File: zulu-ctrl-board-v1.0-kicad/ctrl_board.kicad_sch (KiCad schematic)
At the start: 34 parts, among them J1 Zulu I2C w/ interrupt Connect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, J2 OLED Connector, J305 I2C Qwiic, J5 CENTER_INT, J8 Zulu I2C w/ interrupt Connect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, SW1 SW_SPST, SW2 SW_SPST, SW4 Rotary_Encoder_Switch, U1 PCA9554APW,118

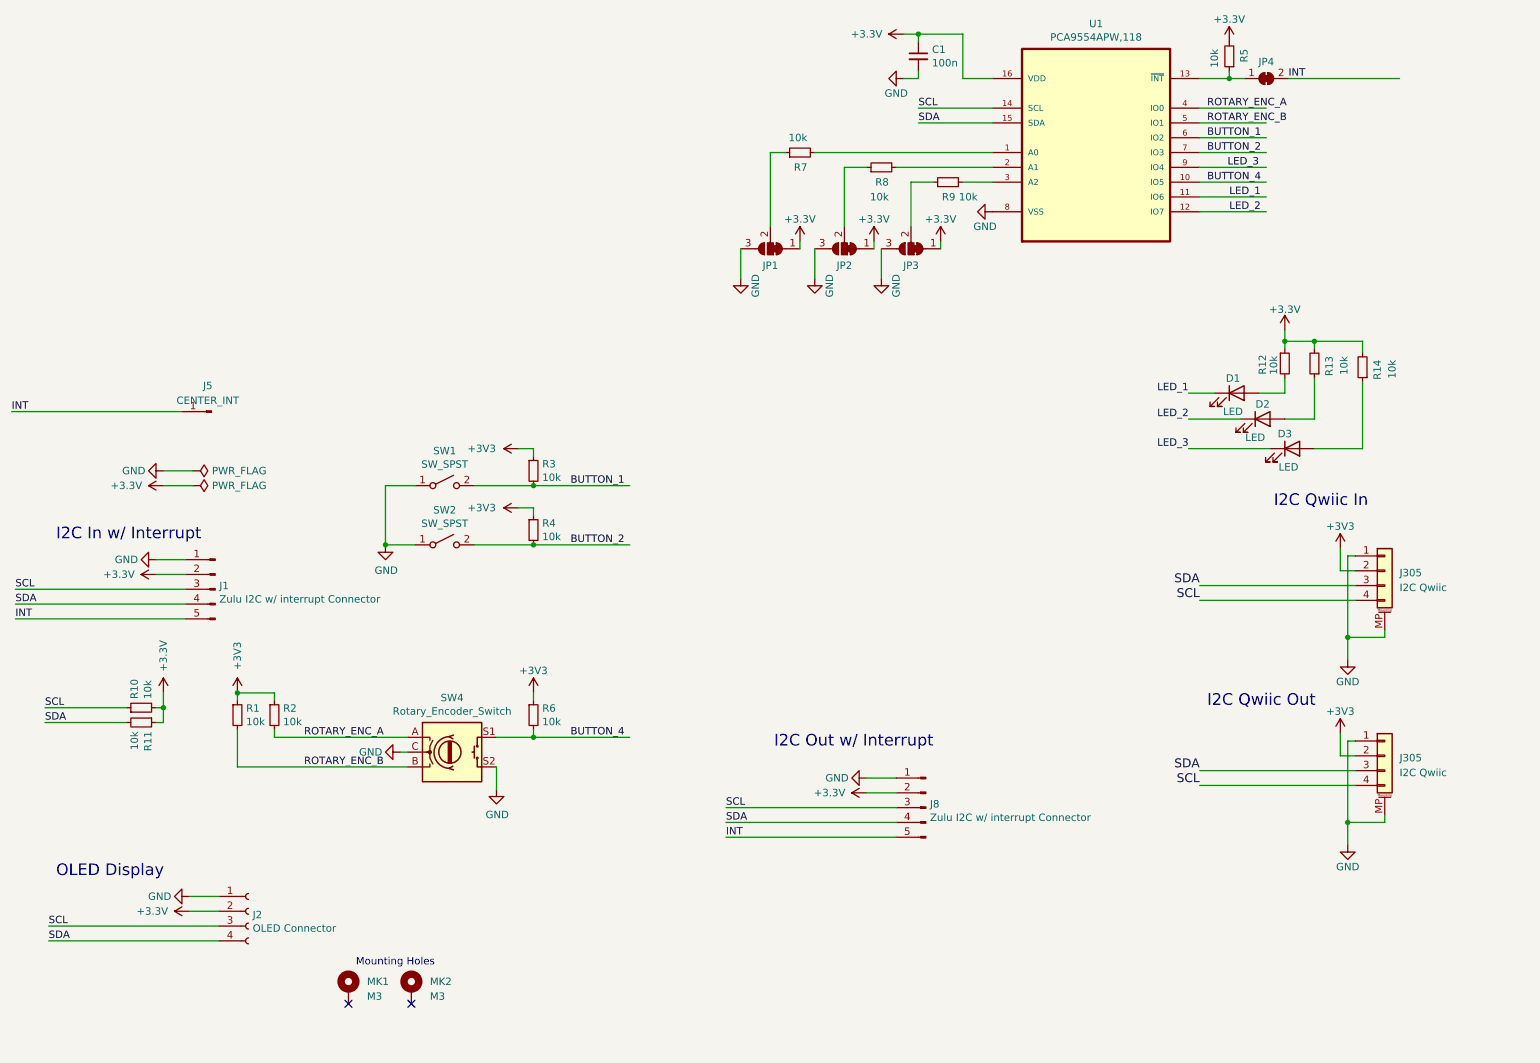
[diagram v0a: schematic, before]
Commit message: Design of new rev
Dropped 2.54mm pitch I2C headers, except for display
Removed LEDs
Added two more mounting holes. Made all 4 of them 2.8mm holes
Decreased the size of the board
Moved buttons, rotary, and screen closer together
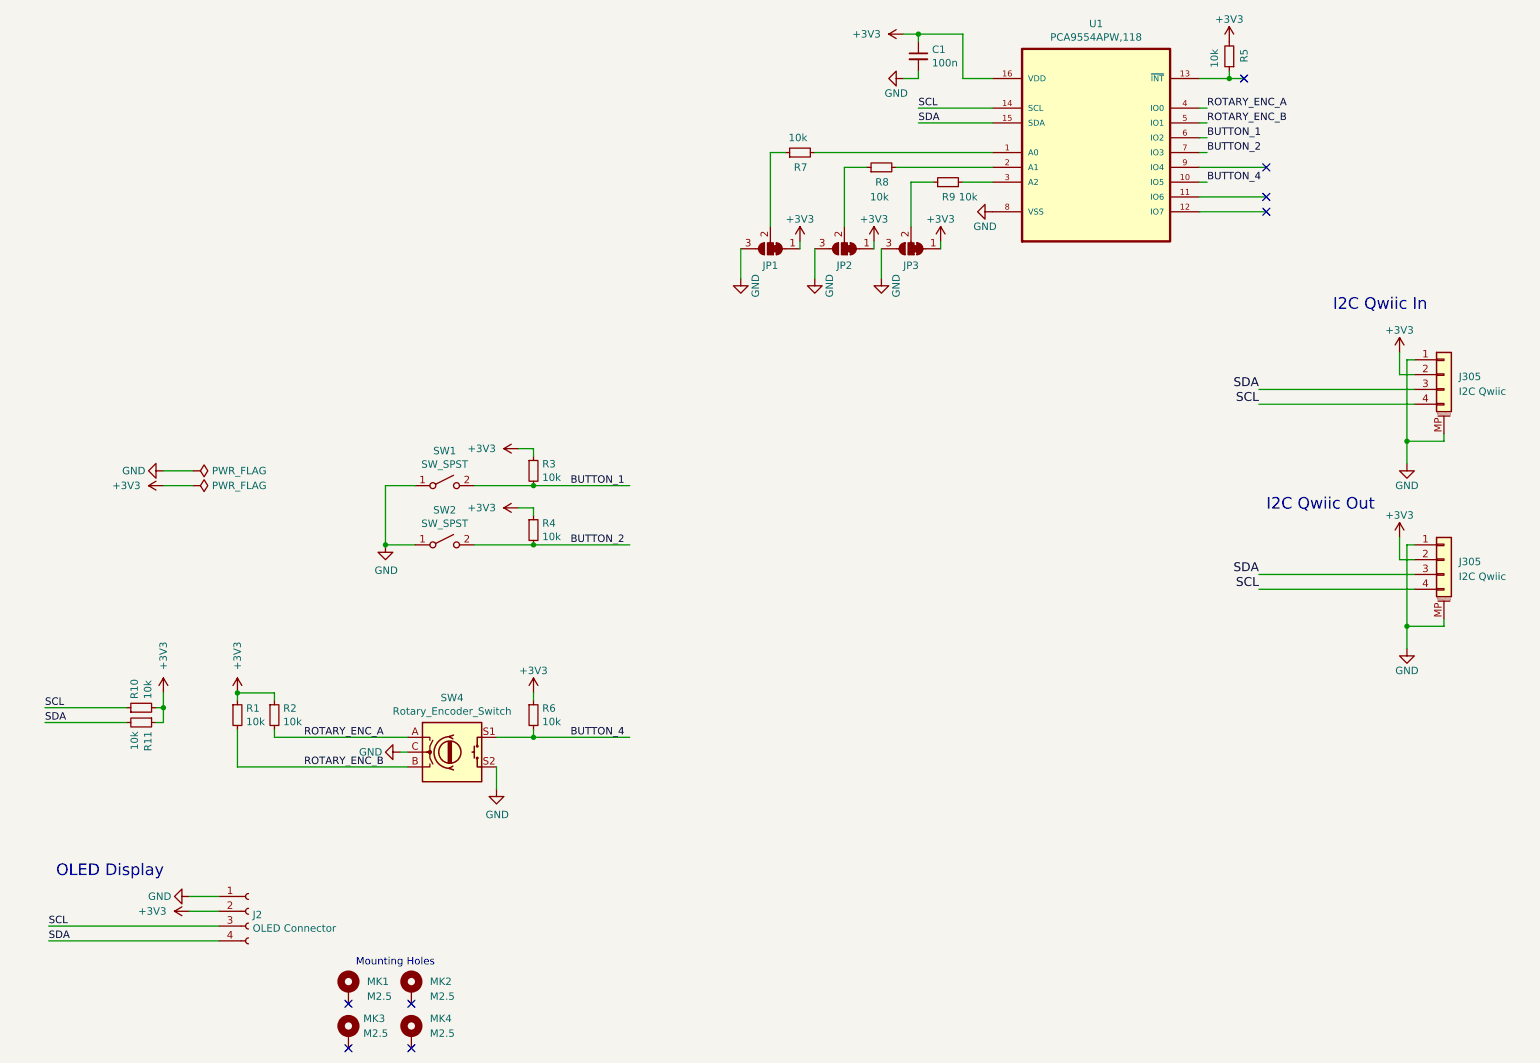
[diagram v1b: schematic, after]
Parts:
- removed D1, D2, D3: LED, LED_THT:LED_D5.0mm, symbol Device:LED
- removed J1, J8: Zulu I2C w/ interrupt Connector, Connector_PinHeader_2.54mm:PinHeader_1x05_P2.54mm_Vertical, symbol Connector:Conn_01x05_Pin
- removed J5: CENTER_INT, Connector_PinHeader_2.54mm:PinHeader_1x01_P2.54mm_Vertical, symbol Connector:Conn_01x01_Pin
- removed JP4: SolderJumper_2_Open, Jumper:SolderJumper-2_P1.3mm_Bridged_RoundedPad1.0x1.5mm, symbol Jumper:SolderJumper_2_Bridged
- removed R12, R13, R14: 10k, Resistor_SMD:R_0805_2012Metric, symbol Device:R_Small
- added MK3, MK4: M2.5, rhc:MountingHole_2.8mm_M2.5custom_DIN965_Pad, symbol Mechanical:MountingHole_Pad
- MK1, MK2: value M3 -> M2.5; footprint MountingHole:MountingHole_3.2mm_M3_Pad -> rhc:MountingHole_2.8mm_M2.5custom_DIN965_Pad
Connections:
- net LED_1: no longer names the net of U1.11 (IO6)
- net LED_2: no longer names the net of U1.12 (IO7)
- net LED_3: no longer names the net of U1.9 (IO4)
- no-connect marks 2 -> 8
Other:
- note removed: "I2C In w/ Interrupt"
- note removed: "I2C Out w/ Interrupt"
- moved on the sheet: J305

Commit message: Add dimensions and create step file
Added dimensions and adjusted some part locations to the nearest 0.1mm
Generated a 3D model step file
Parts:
- removed R5: 10k, Resistor_SMD:R_0805_2012Metric, symbol Device:R_Small
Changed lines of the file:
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@@
 		(color 0 0 0 0)
 	)
-	(junction
-		(at 226.06 26.67)
-		(diameter 0)
-		(color 0 0 0 0)
-	)
 	(no_connect
 		(at 74.93 193.04)
@@
 	)
 	(no_connect
-		(at 228.6 26.67)
+		(at 220.98 26.67)
 	)
 	(no_connect
@@
 	(wire
 		(pts
-			(xy 226.06 26.67) (xy 228.6 26.67)
-		)
-		(stroke
-			(width 0)
-			(type default)
-		)
-	)
-	(wire
-		(pts
 			(xy 154.94 60.96) (xy 154.94 55.88)
 		)
@@
 	(wire
 		(pts
-			(xy 220.98 26.67) (xy 226.06 26.67)
-		)
-		(stroke
-			(width 0)
-			(type default)
-		)
-	)
-	(wire
-		(pts
 			(xy 104.14 90.17) (xy 106.68 90.17)
 		)
@@
 	(wire
 		(pts
-			(xy 226.06 25.4) (xy 226.06 26.67)
-		)
-		(stroke
-			(width 0)
-			(type default)
-		)
-	)
-	(wire
-		(pts
 			(xy 106.68 100.33) (xy 106.68 101.6)
 		)
@@
 	)
 	(symbol
-		(lib_id "Device:R_Small")
-		(at 226.06 22.86 180)
-		(unit 1)
-		(exclude_from_sim no)
-		(in_bom yes)
-		(on_board yes)
-		(dnp no)
-		(property "Reference" "R5"
-			(at 228.6 21.59 90)
-			(effects
-				(font
-					(size 1.27 1.27)
-				)
-				(justify left)
-			)
-		)
-		(property "Value" "10k"
-			(at 223.52 21.59 90)
-			(effects
-				(font
-					(size 1.27 1.27)
-				)
-				(justify left)
-			)
-		)
-		(property "Footprint" "Resistor_SMD:R_0805_2012Metric"
-			(at 226.06 22.86 0)
-			(effects
-				(font
-					(size 1.27 1.27)
-				)
-				(hide yes)
-			)
-		)
-		(property "Datasheet" "~"
-			(at 226.06 22.86 0)
-			(effects
-				(font
-					(size 1.27 1.27)
-				)
-				(hide yes)
-			)
-		)
-		(property "Description" ""
-			(at 226.06 22.86 0)
-			(effects
-				(font
-					(size 1.27 1.27)
-				)
-				(hide yes)
-			)
-		)
-		(property "LCSC" "C17414"
-			(at 226.06 22.86 0)
-			(effects
-				(font
-					(size 1.27 1.27)
-				)
-				(hide yes)
-			)
-		)
-		(pin "1"
-		)
-		(pin "2"
-		)
-		(instances
-			(project "ctrl_board"
-				(path "/a15a7506-eae4-4933-84da-9ad754258706"
-					(reference "R5")
-					(unit 1)
-				)
-			)
-		)
-	)
-	(symbol
 		(lib_id "Mechanical:MountingHole_Pad")
 		(at 74.93 190.5 0)
@@
 					(unit 1)
 				)
-			)
-		)
-	)
-	(symbol
-		(lib_id "power:+3.3V")
-		(at 226.06 20.32 0)
-		(unit 1)
-		(exclude_from_sim no)
-		(in_bom yes)
-		(on_board yes)
-		(dnp no)
-		(property "Reference" "#PWR017"
-			(at 226.06 24.13 0)
-			(effects
-				(font
-					(size 1.27 1.27)
-				)
-				(hide yes)
-			)
-		)
-		(property "Value" "+3V3"
-			(at 226.06 16.51 0)
-			(effects
-				(font
-					(size 1.27 1.27)
-				)
-			)
-		)
-		(property "Footprint" ""
-			(at 226.06 20.32 0)
-			(effects
-				(font
-					(size 1.27 1.27)
-				)
-			)
-		)
-		(property "Datasheet" ""
-			(at 226.06 20.32 0)
-			(effects
-				(font
-					(size 1.27 1.27)
-				)
-			)
-		)
-		(property "Description" ""
-			(at 226.06 20.32 0)
-			(effects
-				(font
-					(size 1.27 1.27)
-				)
-				(hide yes)
-			)
-		)
-		(pin "1"
-		)
-		(instances
-			(project "ctrl_board"
-				(path "/a15a7506-eae4-4933-84da-9ad754258706"
-					(reference "#PWR017")
-					(unit 1)
-				)
